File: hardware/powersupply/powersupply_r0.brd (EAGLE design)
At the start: 160 x 100 mm, 0 parts

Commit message: more basic placement and shape
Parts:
- added IC1, IC2, IC3, IC4: (no value), SparkFun-PowerIC:TO220-IGO
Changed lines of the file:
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@@
 <setting verticaltext="up"/>
 </settings>
-<grid distance="90" unitdist="mm" unit="mm" style="lines" multiple="1" display="yes" altdistance="0.025" altunitdist="inch" altunit="inch"/>
+<grid distance="1" unitdist="mm" unit="mm" style="lines" multiple="1" display="yes" altdistance="0.025" altunitdist="inch" altunit="inch"/>
 <layers>
 <layer number="1" name="Top" color="4" fill="1" visible="yes" active="yes"/>
@@
 <layer number="48" name="Document" color="7" fill="1" visible="yes" active="yes"/>
 <layer number="49" name="Reference" color="7" fill="1" visible="yes" active="yes"/>
+<layer number="50" name="dxf" color="7" fill="1" visible="no" active="no"/>
 <layer number="51" name="tDocu" color="7" fill="1" visible="yes" active="yes"/>
 <layer number="52" name="bDocu" color="7" fill="1" visible="yes" active="yes"/>
+<layer number="53" name="tGND_GNDA" color="7" fill="9" visible="no" active="no"/>
+<layer number="54" name="bGND_GNDA" color="1" fill="9" visible="no" active="no"/>
+<layer number="56" name="wert" color="7" fill="1" visible="no" active="no"/>
 <layer number="91" name="Nets" color="2" fill="1" visible="no" active="no"/>
 <layer number="92" name="Busses" color="1" fill="1" visible="no" active="no"/>
@@
 <layer number="97" name="Info" color="7" fill="1" visible="no" active="no"/>
 <layer number="98" name="Guide" color="6" fill="1" visible="no" active="no"/>
+<layer number="100" name="Muster" color="7" fill="1" visible="no" active="no"/>
+<layer number="101" name="Patch_Top" color="12" fill="4" visible="yes" active="yes"/>
+<layer number="102" name="Vscore" color="7" fill="1" visible="yes" active="yes"/>
+<layer number="103" name="tMap" color="7" fill="1" visible="yes" active="yes"/>
+<layer number="104" name="Name" color="16" fill="1" visible="yes" active="yes"/>
+<layer number="105" name="tPlate" color="7" fill="1" visible="yes" active="yes"/>
+<layer number="106" name="bPlate" color="7" fill="1" visible="yes" active="yes"/>
+<layer number="107" name="Crop" color="7" fill="1" visible="yes" active="yes"/>
+<layer number="108" name="tplace-old" color="10" fill="1" visible="yes" active="yes"/>
+<layer number="109" name="ref-old" color="11" fill="1" visible="yes" active="yes"/>
+<layer number="116" name="Patch_BOT" color="9" fill="4" visible="yes" active="yes"/>
+<layer number="121" name="_tsilk" color="7" fill="1" visible="yes" active="yes"/>
+<layer number="122" name="_bsilk" color="7" fill="1" visible="yes" active="yes"/>
+<layer number="125" name="_tNames" color="7" fill="1" visible="yes" active="yes"/>
+<layer number="144" name="Drill_legend" color="7" fill="1" visible="yes" active="yes"/>
+<layer number="151" name="HeatSink" color="7" fill="1" visible="yes" active="yes"/>
+<layer number="199" name="Contour" color="7" fill="1" visible="yes" active="yes"/>
+<layer number="200" name="200bmp" color="1" fill="10" visible="yes" active="yes"/>
+<layer number="201" name="201bmp" color="2" fill="10" visible="yes" active="yes"/>
+<layer number="202" name="202bmp" color="3" fill="10" visible="yes" active="yes"/>
+<layer number="203" name="203bmp" color="4" fill="10" visible="yes" active="yes"/>
+<layer number="204" name="204bmp" color="5" fill="10" visible="yes" active="yes"/>
+<layer number="205" name="205bmp" color="6" fill="10" visible="yes" active="yes"/>
+<layer number="206" name="206bmp" color="7" fill="10" visible="yes" active="yes"/>
+<layer number="207" name="207bmp" color="8" fill="10" visible="yes" active="yes"/>
+<layer number="208" name="208bmp" color="9" fill="10" visible="yes" active="yes"/>
+<layer number="209" name="209bmp" color="7" fill="1" visible="yes" active="yes"/>
+<layer number="210" name="210bmp" color="7" fill="1" visible="yes" active="yes"/>
+<layer number="211" name="211bmp" color="7" fill="1" visible="yes" active="yes"/>
+<layer number="212" name="212bmp" color="7" fill="1" visible="yes" active="yes"/>
+<layer number="213" name="213bmp" color="7" fill="1" visible="yes" active="yes"/>
+<layer number="214" name="214bmp" color="7" fill="1" visible="yes" active="yes"/>
+<layer number="215" name="215bmp" color="7" fill="1" visible="yes" active="yes"/>
+<layer number="216" name="216bmp" color="7" fill="1" visible="yes" active="yes"/>
+<layer number="217" name="217bmp" color="18" fill="1" visible="no" active="no"/>
+<layer number="218" name="218bmp" color="19" fill="1" visible="no" active="no"/>
+<layer number="219" name="219bmp" color="20" fill="1" visible="no" active="no"/>
+<layer number="220" name="220bmp" color="21" fill="1" visible="no" active="no"/>
+<layer number="221" name="221bmp" color="22" fill="1" visible="no" active="no"/>
+<layer number="222" name="222bmp" color="23" fill="1" visible="no" active="no"/>
+<layer number="223" name="223bmp" color="24" fill="1" visible="no" active="no"/>
+<layer number="224" name="224bmp" color="25" fill="1" visible="no" active="no"/>
+<layer number="250" name="Descript" color="3" fill="1" visible="no" active="no"/>
+<layer number="251" name="SMDround" color="12" fill="11" visible="no" active="no"/>
+<layer number="254" name="cooling" color="7" fill="1" visible="yes" active="yes"/>
 </layers>
 <board>
@@
 <wire x1="0" y1="100" x2="0" y2="0" width="0" layer="20"/>
 <wire x1="90" y1="0" x2="0" y2="90" width="0.4064" layer="21"/>
-<wire x1="2" y1="102" x2="2" y2="-4" width="0.4064" layer="21"/>
+<wire x1="2" y1="102" x2="2" y2="84" width="0.4064" layer="21"/>
+<wire x1="2" y1="84" x2="2" y2="-4" width="0.4064" layer="21"/>
 <wire x1="-4" y1="2" x2="92" y2="2" width="0.4064" layer="21"/>
-<wire x1="86" y1="0" x2="0" y2="86" width="0.4064" layer="21"/>
+<wire x1="86" y1="0" x2="2" y2="84" width="0.4064" layer="21"/>
+<wire x1="2" y1="84" x2="0" y2="86" width="0.4064" layer="21"/>
 <wire x1="32" y1="0" x2="0" y2="32" width="0.4064" layer="21"/>
 <wire x1="40" y1="0" x2="0" y2="40" width="0.4064" layer="21"/>
-<wire x1="0" y1="0" x2="90" y2="90" width="0.4064" layer="21"/>
+<wire x1="0" y1="0" x2="32" y2="32" width="0.4064" layer="21"/>
+<wire x1="32" y1="32" x2="55" y2="55" width="0.4064" layer="21"/>
+<wire x1="55" y1="55" x2="90" y2="90" width="0.4064" layer="21"/>
+<wire x1="32" y1="32" x2="32" y2="64" width="0.4064" layer="21"/>
+<wire x1="32" y1="32" x2="64" y2="32" width="0.4064" layer="21"/>
+<circle x="45" y="45" radius="18.384775" width="0.4064" layer="21"/>
+<wire x1="55" y1="55" x2="55" y2="110" width="0.4064" layer="21"/>
+<wire x1="55" y1="55" x2="110" y2="55" width="0.4064" layer="21"/>
+<wire x1="2" y1="84" x2="55" y2="55" width="0.4064" layer="21"/>
+<wire x1="86" y1="0" x2="55" y2="55" width="0.4064" layer="21"/>
 </plain>
 <attributes>
@@
 </autorouter>
 <elements>
+<element name="IC1" library="SparkFun-PowerIC" package="TO220-IGO" value="" x="50" y="4" rot="R180"/>
+<element name="IC2" library="SparkFun-PowerIC" package="TO220-IGO" value="" x="70" y="4" rot="R180"/>
+<element name="IC3" library="SparkFun-PowerIC" package="TO220-IGO" value="" x="6" y="48" rot="R90"/>
+<element name="IC4" library="SparkFun-PowerIC" package="TO220-IGO" value="" x="6" y="68" rot="R90"/>
 </elements>
 <signals>

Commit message: basic placement
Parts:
- added C1, C2: (no value), SparkFun-Passives:CPOL-RADIAL-1000UF-25V
- added C3, C4, C5, C6: (no value), SparkFun-Passives:CPOL-RADIAL-100UF-25V
- added F1, F2, F3, F4, F5: FUSEX20MM, SparkFun-Passives:FUSE_5MM
- added U$1, U$2, U$3, U$4, U$5: SCREWTERMINAL-2PIN, openct:SCREWTERMINAL-2PIN
- moved IC2 2.83 mm to (72.0, 6.00)
- moved IC1 2.00 mm to (50.0, 6.00)
- moved IC4 2.00 mm to (6.00, 70.0)
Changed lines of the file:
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@@
 <wire x1="2" y1="84" x2="55" y2="55" width="0.4064" layer="21"/>
 <wire x1="86" y1="0" x2="55" y2="55" width="0.4064" layer="21"/>
+<wire x1="2" y1="84" x2="86" y2="0" width="0.4064" layer="21" curve="-64.942385"/>
+<wire x1="0" y1="90" x2="90" y2="0" width="0.4064" layer="21" curve="-90"/>
 </plain>
 <attributes>
@@
 </autorouter>
 <elements>
-<element name="IC1" library="SparkFun-PowerIC" package="TO220-IGO" value="" x="50" y="4" rot="R180"/>
-<element name="IC2" library="SparkFun-PowerIC" package="TO220-IGO" value="" x="70" y="4" rot="R180"/>
+<element name="IC1" library="SparkFun-PowerIC" package="TO220-IGO" value="" x="50" y="6" rot="R180"/>
+<element name="IC2" library="SparkFun-PowerIC" package="TO220-IGO" value="" x="72" y="6" rot="R180"/>
 <element name="IC3" library="SparkFun-PowerIC" package="TO220-IGO" value="" x="6" y="48" rot="R90"/>
-<element name="IC4" library="SparkFun-PowerIC" package="TO220-IGO" value="" x="6" y="68" rot="R90"/>
+<element name="IC4" library="SparkFun-PowerIC" package="TO220-IGO" value="" x="6" y="70" rot="R90"/>
+<element name="U$1" library="openct" package="SCREWTERMINAL-2PIN" value="SCREWTERMINAL-2PIN" x="3" y="-8"/>
+<element name="U$2" library="openct" package="SCREWTERMINAL-2PIN" value="SCREWTERMINAL-2PIN" x="3" y="-19"/>
+<element name="U$3" library="openct" package="SCREWTERMINAL-2PIN" value="SCREWTERMINAL-2PIN" x="3" y="-30"/>
+<element name="U$4" library="openct" package="SCREWTERMINAL-2PIN" value="SCREWTERMINAL-2PIN" x="3" y="-41"/>
+<element name="U$5" library="openct" package="SCREWTERMINAL-2PIN" value="SCREWTERMINAL-2PIN" x="22.560659375" y="22.646446875" rot="R135"/>
+<element name="F1" library="SparkFun-Passives" package="FUSE_5MM" value="FUSEX20MM" x="54.79289375" y="23.707103125"/>
+<element name="F2" library="SparkFun-Passives" package="FUSE_5MM" value="FUSEX20MM" x="76.20710625" y="23.878678125"/>
+<element name="F3" library="SparkFun-Passives" package="FUSE_5MM" value="FUSEX20MM" x="24" y="53" rot="R90"/>
+<element name="F4" library="SparkFun-Passives" package="FUSE_5MM" value="FUSEX20MM" x="24" y="74.5" rot="R90"/>
+<element name="C1" library="SparkFun-Passives" package="CPOL-RADIAL-1000UF-25V" value="" x="34" y="15"/>
+<element name="C2" library="SparkFun-Passives" package="CPOL-RADIAL-1000UF-25V" value="" x="15" y="34"/>
+<element name="F5" library="SparkFun-Passives" package="FUSE_5MM" value="FUSEX20MM" x="31.5" y="31.5" rot="R225"/>
+<element name="C3" library="SparkFun-Passives" package="CPOL-RADIAL-100UF-25V" value="" x="-8" y="-43"/>
+<element name="C4" library="SparkFun-Passives" package="CPOL-RADIAL-100UF-25V" value="" x="-15" y="-43"/>
+<element name="C5" library="SparkFun-Passives" package="CPOL-RADIAL-100UF-25V" value="" x="-22" y="-43"/>
+<element name="C6" library="SparkFun-Passives" package="CPOL-RADIAL-100UF-25V" value="" x="-29" y="-43"/>
 </elements>
 <signals>

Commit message: component layout complete
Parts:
- removed U$2, U$3, U$4: SCREWTERMINAL-2PIN, openct:SCREWTERMINAL-2PIN
- added C7: (no value), SparkFun-Passives:CPOL-RADIAL-100UF-25V
- added CN17: 22-23-2041, con-molex:22-23-2041
- added JP1, JP3: M02JST-PTH-VERT, SparkFun-Connectors:JST-2-PTH-VERT
- added U$6: CON-USB, openct:MOLEX-USB-105057-0001
- moved C6 119.1 mm to (19.0, 66.0), turned to 90 degrees
- moved C4 102.0 mm to (66.0, 19.0)
- moved C5 98.0 mm to (19.0, 46.0), turned to 90 degrees
- moved U$1 86.3 mm to (57.4, 59.0), turned to 315 degrees
- moved C3 81.6 mm to (45.0, 19.0)
- moved F5 9.90 mm to (38.5, 38.5)
- moved F4 4.12 mm to (25.0, 78.5), turned to 270 degrees
- moved F3 3.16 mm to (25.0, 56.0), turned to 270 degrees
- moved F2 2.50 mm to (78.2, 25.4)
- moved IC3 2.00 mm to (6.00, 50.0)
- moved IC4 2.00 mm to (6.00, 72.0)
- moved F1 1.80 mm to (55.8, 25.2)
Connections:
- new net GND: C3.2, C4.2, C5.2, C6.2, C7.2, CN17.2, CN17.3, IC1.GND, IC2.GND, IC3.GND, IC4.GND, U$1.2
- new net N$1: C3.1, F1.1, IC1.OUT
- new net N$2: C4.1, F2.1, IC2.OUT
- new net N$3: C5.1, F3.1, IC3.OUT
- new net N$4: C6.1, F4.1, IC4.OUT
- new net N$5: CN17.4, F4.3
- new net VBIAS: C7.1, CN17.1, U$1.1

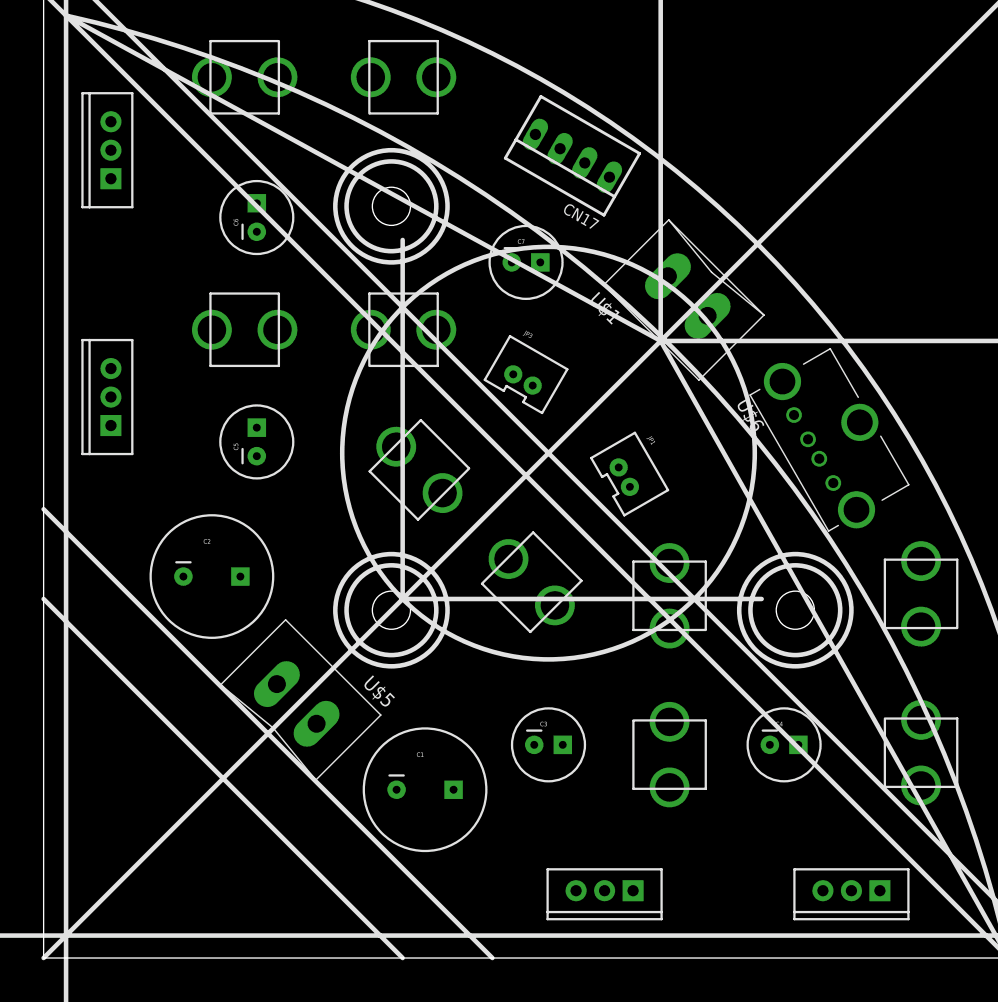
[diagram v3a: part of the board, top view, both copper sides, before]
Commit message: major routing on power supply board
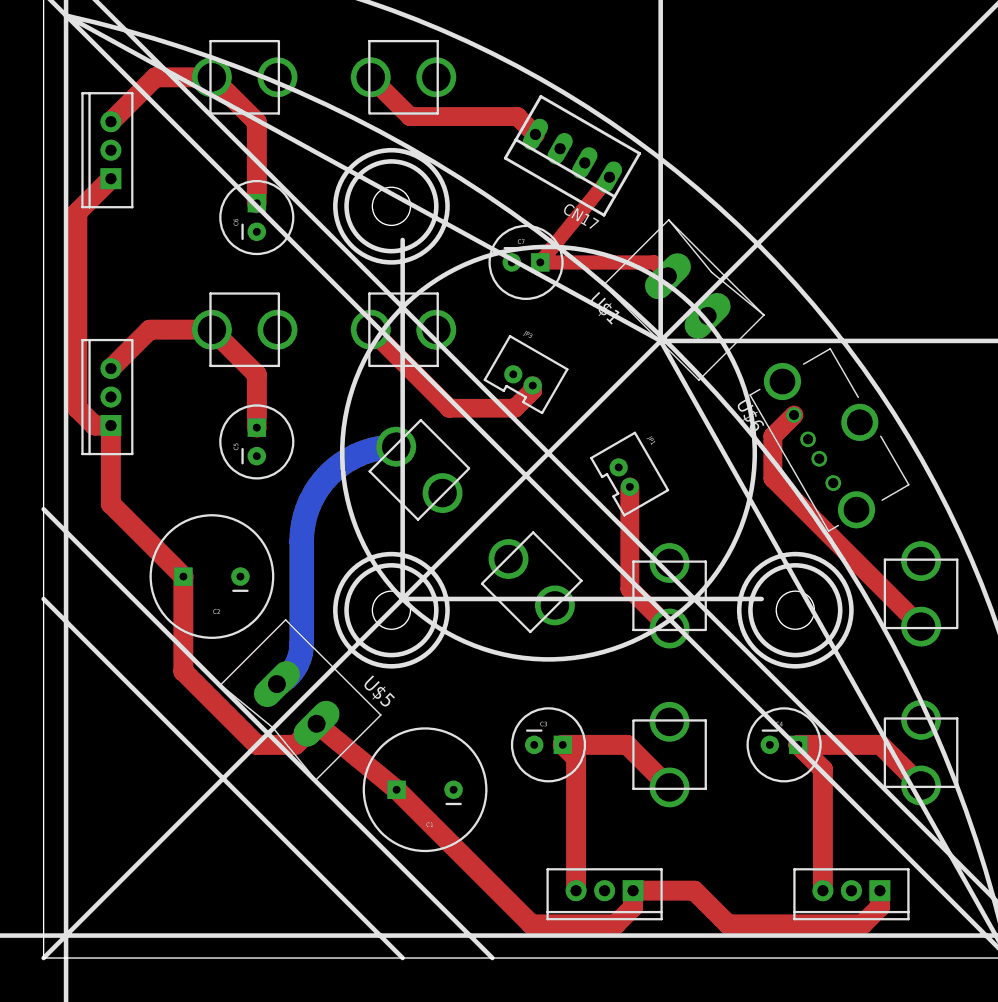
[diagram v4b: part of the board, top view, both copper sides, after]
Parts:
- turned C1 to 180 degrees
- turned C2 to 180 degrees
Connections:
- new net N$10: F3.3, JP3.2
- new net N$11: C1.1, C2.1, IC1.IN, IC2.IN, IC3.IN, IC4.IN, U$5.1
- new net N$7: F5.1, U$5.2
- new net N$8: F1.3, JP1.2
- new net N$9: F2.3, U$6.1
- net GND: now also C1.2, C2.2, F5.3, JP1.1, JP3.1, U$6.4
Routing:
- net N$11: track 0.00 -> 128.0 mm
- net N$2: track 0.00 -> 26.3 mm
- net N$7: track 0.00 -> 25.3 mm
- net N$9: track 0.00 -> 25.1 mm
- net N$1: track 0.00 -> 24.6 mm
- net N$4: track 0.00 -> 23.5 mm
- net VBIAS: track 0.00 -> 21.7 mm
- net N$3: track 0.00 -> 20.8 mm
- net N$10: track 0.00 -> 18.4 mm
- net N$5: track 0.00 -> 16.8 mm
- net N$8: track 0.00 -> 14.1 mm
